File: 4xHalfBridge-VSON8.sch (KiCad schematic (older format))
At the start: 78 parts, among them U1 VSON8_Nexfet, U2 VSON8_Nexfet, U3 VSON8_Nexfet, U4 VSON8_Nexfet, U5 VSON8_Nexfet, U6 VSON8_Nexfet, U7 VSON8_Nexfet, U8 VSON8_Nexfet, U9 PowerStage_L

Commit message: continue routing
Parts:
- removed C35: C, Capacitor_SMD:C_1206_3216Metric_Pad1.42x1.75mm_HandSolder, symbol Device:C
- removed C36: C, Capacitor_SMD:C_0805_2012Metric_Pad1.15x1.40mm_HandSolder, symbol Device:C
- renumbered C4 to C1, C17 to C10, C27 to C11, C18 to C12, C19 to C13, C20 to C14, C2 to C15, C6 to C16, C13 to C17, C26 to C18, C14 to C19, C5 to C2, C15 to C20, C16 to C21, C29 to C22, C30 to C23, C31 to C24, C3 to C25, C8 to C26, C32 to C27, C21 to C28, C33 to C29, C9 to C3, C28 to C30, C34 to C31, C22 to C32, C23 to C33, C24 to C34, C25 to C4, C10 to C5, C11 to C6, C12 to C7, C1 to C8, C7 to C9, R6 to R1, R19 to R10, R3 to R11, R14 to R12, R26 to R13, R22 to R14, R2 to R15, R10 to R16, R18 to R17, R4 to R18, R13 to R19, R9 to R2, R25 to R20, R29 to R21, R21 to R22, R30 to R23, R5 to R24, R15 to R25, R23 to R26, R7 to R27, R16 to R28, R28 to R29, R17 to R3, R27 to R30, R8 to R4, R12 to R5, R24 to R6, R20 to R7, R1 to R8, R11 to R9, U4 to U1, U5 to U2, U9 to U3, U1 to U4, U7 to U5, U2 to U6, U6 to U7, U3 to U8, U8 to U9
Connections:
- wire segments 145 -> 146

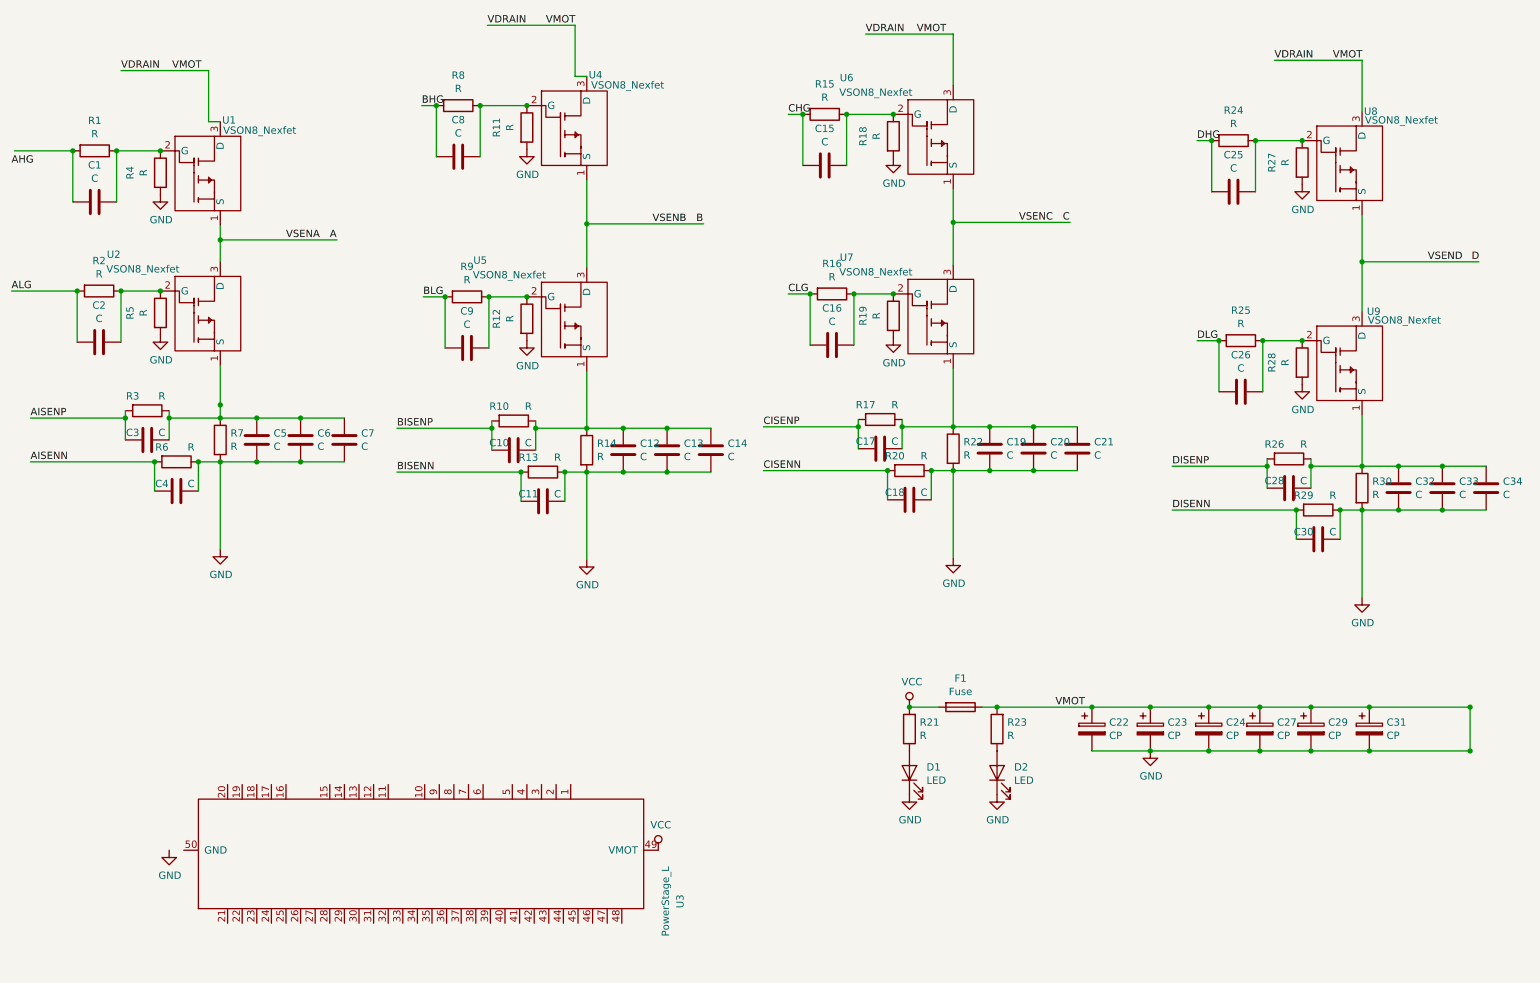
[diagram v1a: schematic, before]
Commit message: finalize pcb without eeprom
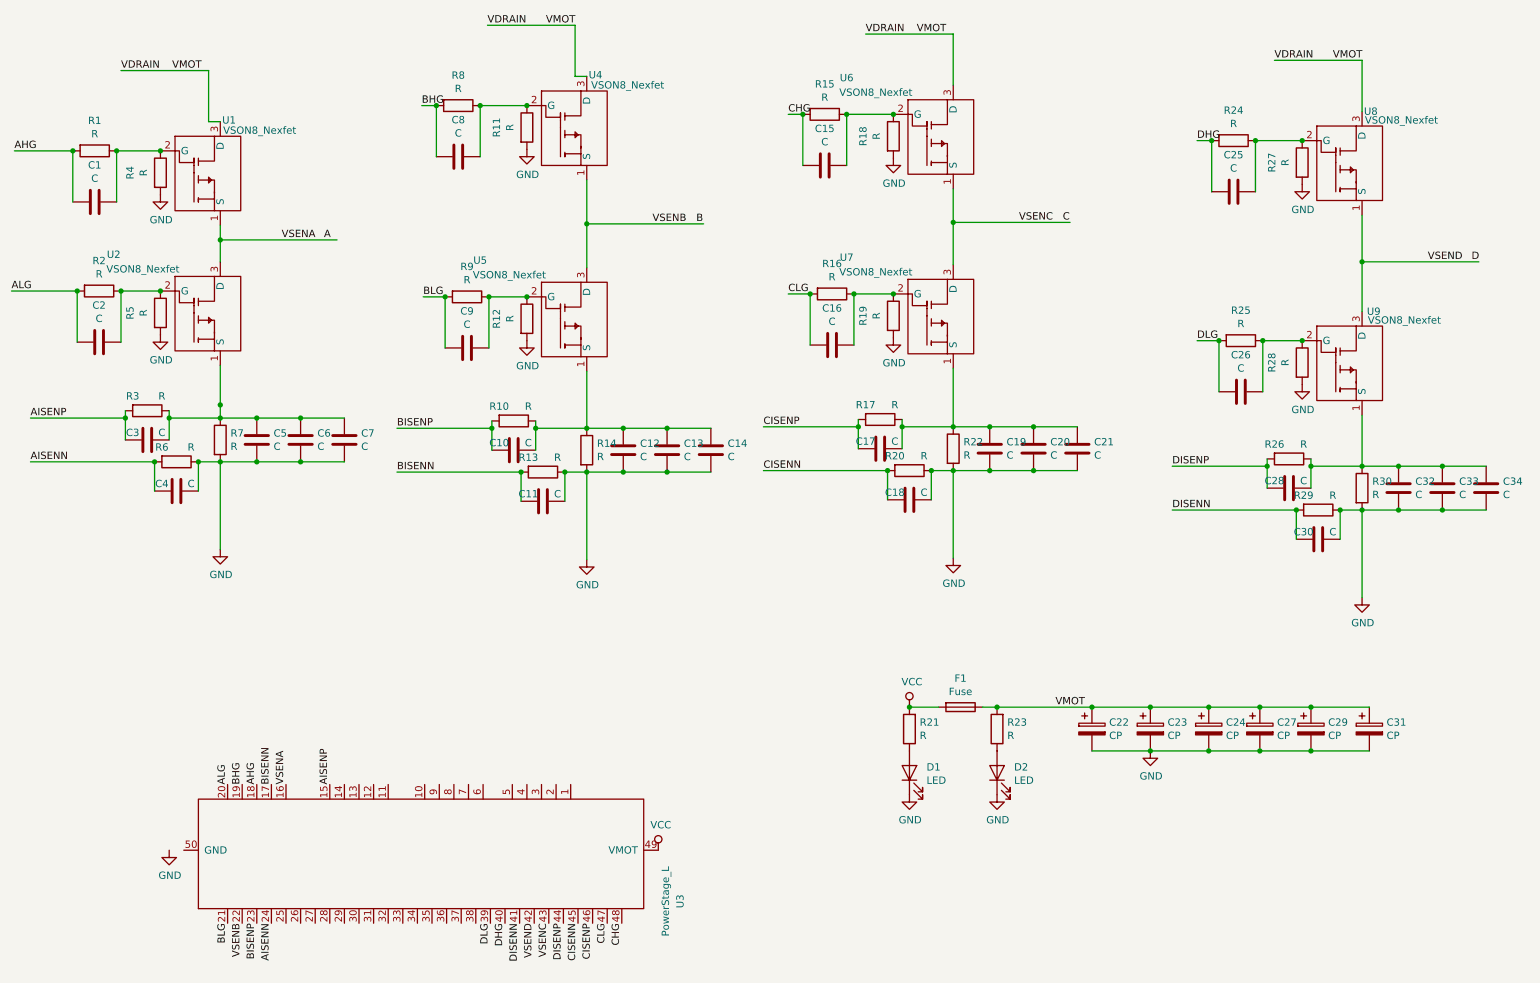
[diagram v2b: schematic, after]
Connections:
- wire segments 146 -> 141
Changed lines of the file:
@@
 Wire Wire Line
 	9800 5300 9400 5300
-Connection ~ 9800 5300
 Connection ~ 9400 5300
 Wire Wire Line
 	9800 5600 9400 5600
-Connection ~ 9800 5600
 Connection ~ 9400 5600
 Wire Wire Line
@@
 Wire Wire Line
 	520  1490 920  1490
-Text Label 500  1590 0    50   ~ 0
+Text Label 520  1490 0    50   ~ 0
 AHG
 Connection ~ 1220 1490
@@
 	0    1    1    0
 $EndComp
-Text Label 2380 2100 0    50   ~ 0
+Text Label 2350 2100 0    50   ~ 0
 VSENA
-Text Label 2680 2100 0    50   ~ 0
+Text Label 2640 2100 0    50   ~ 0
 A
 Wire Wire Line
@@
 Wire Wire Line
 	1480 3620 1480 3820
-Wire Wire Line
-	9800 5600 10490 5600
-Wire Wire Line
-	10490 5600 10490 5300
-Wire Wire Line
-	9800 5300 10490 5300
-Connection ~ 10490 5600
-Wire Wire Line
-	10490 5600 10500 5600
-Connection ~ 10490 5300
-Wire Wire Line
-	10490 5300 10500 5300
 $Comp
 L power:GND #PWR0101
@@
 	1    0    0    -1
 $EndComp
+Text Label 2280 5830 1    50   ~ 0
+BISENN
+Text Label 2180 6780 3    50   ~ 0
+BISENP
+Text Label 2080 6780 3    50   ~ 0
+VSENB
+Text Label 1980 6780 3    50   ~ 0
+BLG
+Text Label 2080 5830 1    50   ~ 0
+BHG
+Text Label 1980 5830 1    50   ~ 0
+ALG
+Text Label 2280 6780 3    50   ~ 0
+AISENN
+Text Label 2180 5830 1    50   ~ 0
+AHG
+Text Label 2680 5830 1    50   ~ 0
+AISENP
+Text Label 2380 5830 1    50   ~ 0
+VSENA
+Text Label 4580 6780 3    50   ~ 0
+CLG
+Text Label 4680 6780 3    50   ~ 0
+CHG
+Text Label 4380 6780 3    50   ~ 0
+CISENN
+Text Label 4480 6780 3    50   ~ 0
+CISENP
+Text Label 4180 6780 3    50   ~ 0
+VSENC
+Text Label 3980 6780 3    50   ~ 0
+DISENN
+Text Label 4280 6780 3    50   ~ 0
+DISENP
+Text Label 4080 6780 3    50   ~ 0
+VSEND
+Text Label 3880 6780 3    50   ~ 0
+DHG
+Text Label 3780 6780 3    50   ~ 0
+DLG
 $EndSCHEMATC

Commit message: finalize schematic and PCB
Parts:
- renumbered C8 to C1, C5 to C10, C6 to C11, C7 to C12, C17 to C13, C19 to C14, C20 to C15, C21 to C16, C10 to C17, C12 to C18, C13 to C19, C15 to C2, C14 to C20, C28 to C21, C32 to C22, C33 to C23, C34 to C24, C4 to C25, C18 to C26, C11 to C27, C30 to C28, C22 to C29, C25 to C3, C23 to C30, C24 to C31, C27 to C32, C29 to C33, C31 to C34, C1 to C4, C2 to C5, C16 to C6, C9 to C7, C26 to C8, C3 to C9, R8 to R1, R16 to R10, R9 to R11, R5 to R12, R19 to R13, R12 to R14, R25 to R15, R28 to R16, R3 to R17, R17 to R18, R10 to R19, R15 to R2, R7 to R20, R22 to R21, R14 to R22, R26 to R23, R6 to R24, R20 to R25, R13 to R26, R30 to R27, R29 to R28, R21 to R29, R11 to R3, R23 to R30, R18 to R4, R24 to R5, R1 to R6, R27 to R7, R4 to R8, R2 to R9, U4 to U1, U6 to U2, U8 to U3, U1 to U4, U2 to U5, U7 to U6, U5 to U7, U9 to U8, U3 to U9
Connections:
- net labels added: 5V, SCL, SDA, WP
- wire segments 141 -> 150
